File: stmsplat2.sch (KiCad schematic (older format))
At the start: 97 parts, among them J1 C11_2X36, J10 Conn_01x03_Male, J11 Conn_01x02_Male, J12 Conn_01x04_Male, J13 Conn_01x04_Male, J14 Conn_01x02, J15 Conn_01x02, J16 Screw_Terminal_01x03, J17 Screw_Terminal_01x02, J2 C12_2X36, J3 Conn_01x04_Male, J4 Conn_01x04_Male, J5 Conn_Coaxial, J6 Conn_01x06, J7 Conn_01x04_Male, J8 Conn_01x04_Male, J9 Conn_01x03_Male, Q1 BSS138LT1G, U1 ublox_chinese_PCB_module, U10 XCVR_E30-400M20S, U2 ESP32-C3-13, U3 SST25VF032B, U4 48L512-48LM01, U5 Opamp_Quad_MCP6024, U6 E180-ZG120A, U7 AZ1084C, U8 MCP6S93-X_UN, U9 DS2485

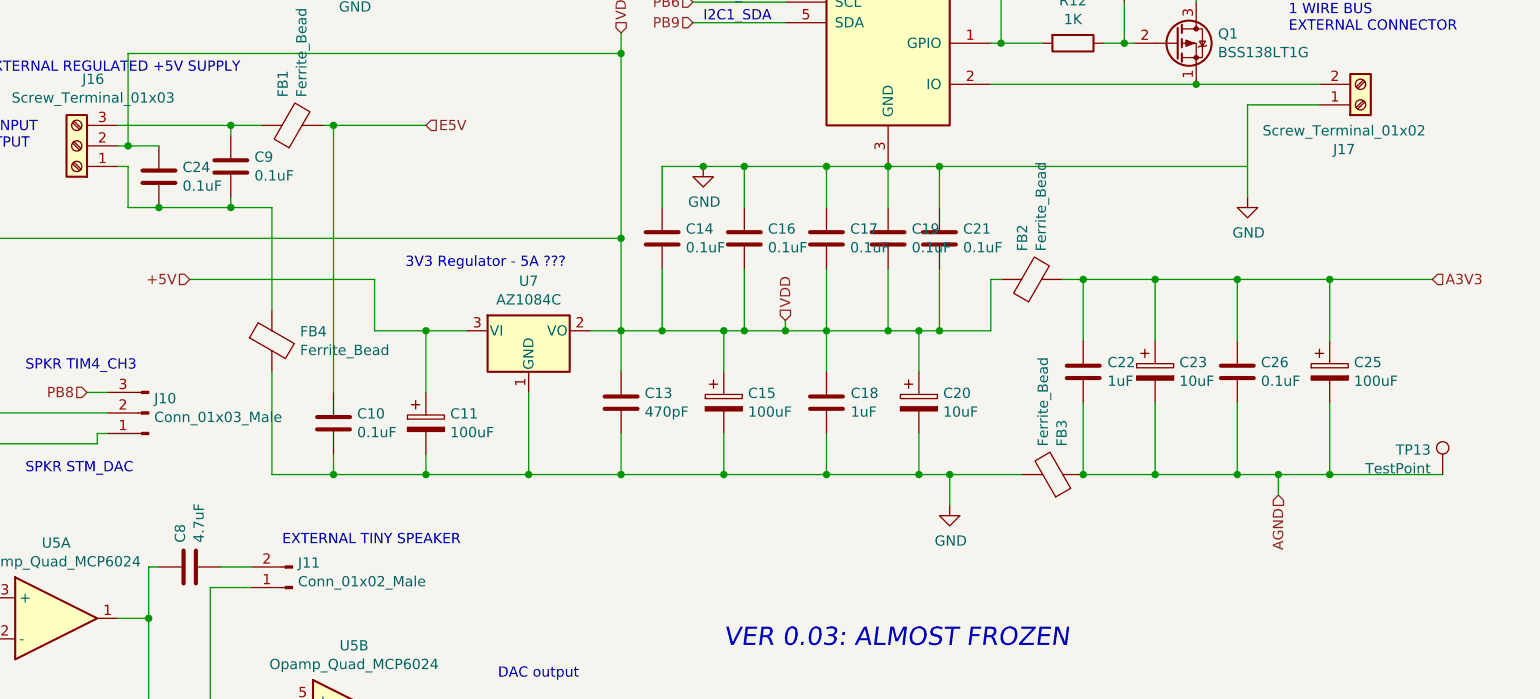
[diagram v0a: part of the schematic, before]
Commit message: changed all 0603 footprints to 0805 in the schematic
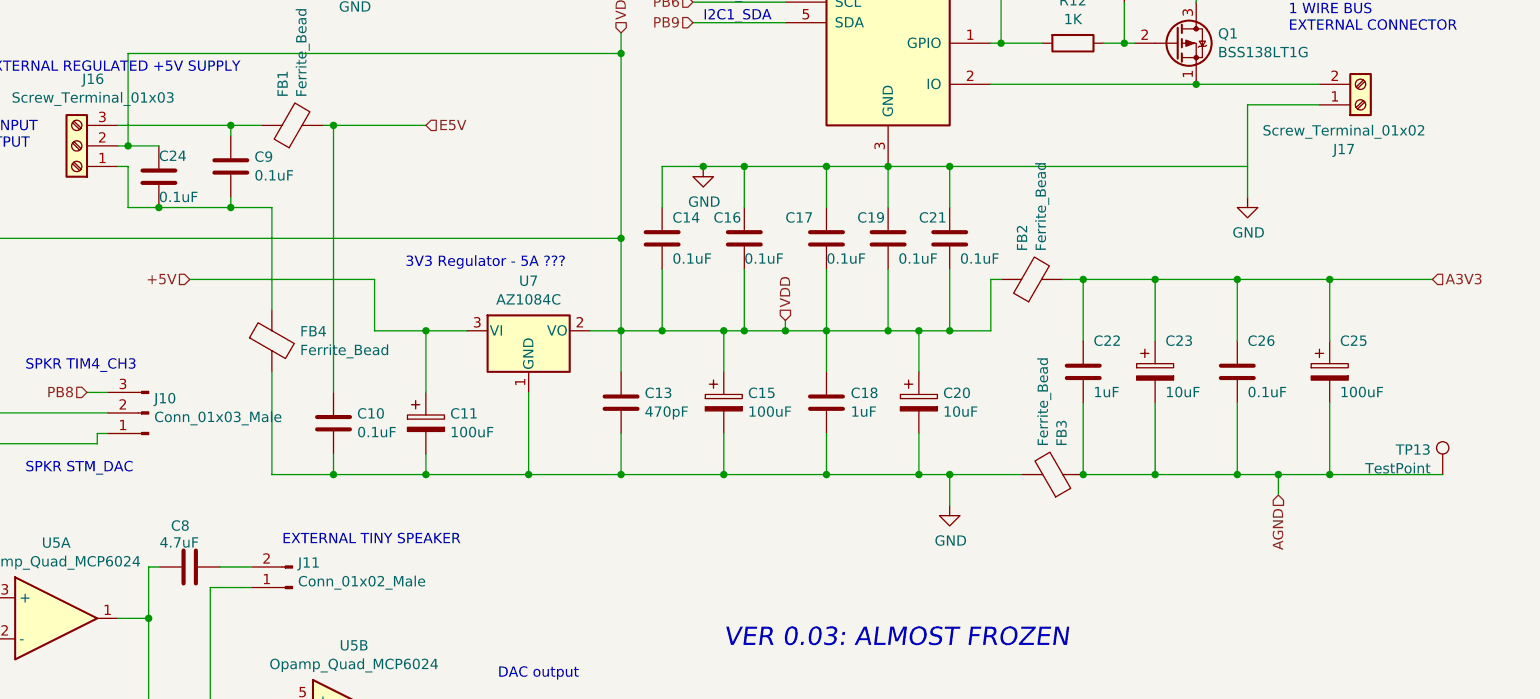
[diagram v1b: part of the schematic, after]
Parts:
- C1, C10, C14, C16, C17, C19, C21: footprint Capacitor_SMD:C_0603_1608Metric -> Capacitor_SMD:C_0805_2012Metric
- R1, R10, R11, R12, R13, R14, R2, R4, R7, R8, R9: footprint Resistor_SMD:R_0603_1608Metric -> Resistor_SMD:R_0805_2012Metric
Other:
- moved on the sheet: C21
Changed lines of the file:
@@
 U 1 1 5BE7E7BD
 P 14300 8950
-F 0 "C23" H 14418 8996 50  0000 L CNN
-F 1 "10uF" H 14418 8905 50  0000 L CNN
+F 0 "C23" H 14350 9100 50  0000 L CNN
+F 1 "10uF" H 14350 8850 50  0000 L CNN
 F 2 "Capacitor_THT:CP_Radial_D5.0mm_P2.50mm" H 14338 8800 50  0001 C CNN
 F 3 "~" H 14300 8950 50  0001 C CNN
@@
 U 1 1 5C39DBA4
 P 9600 9900
-F 0 "C8" H 9718 9946 50  0000 L CNN
-F 1 "4.7uF" H 9718 9855 50  0000 L CNN
+F 0 "C8" V 9800 9900 50  0000 L CNN
+F 1 "4.7uF" V 9718 9855 50  0000 L CNN
 F 2 "Capacitor_SMD:C_0805_2012Metric" H 9638 9750 50  0001 C CNN
 F 3 "~" H 9600 9900 50  0001 C CNN
@@
 F 0 "R13" H 14220 7046 50  0000 L CNN
 F 1 "100K" H 14220 6955 50  0000 L CNN
-F 2 "Resistor_SMD:R_0603_1608Metric" V 14080 7000 50  0001 C CNN
+F 2 "Resistor_SMD:R_0805_2012Metric" V 14080 7000 50  0001 C CNN
 F 3 "~" H 14150 7000 50  0001 C CNN
 	1    14150 7000
@@
 F 0 "R12" V 13693 7350 50  0000 C CNN
 F 1 "1K" V 13784 7350 50  0000 C CNN
-F 2 "Resistor_SMD:R_0603_1608Metric" V 13830 7350 50  0001 C CNN
+F 2 "Resistor_SMD:R_0805_2012Metric" V 13830 7350 50  0001 C CNN
 F 3 "~" H 13900 7350 50  0001 C CNN
 	1    13900 7350
@@
 SPI3 TRACKS TO BE KEPT SHORT AND EQUAL LENGTH
 Wire Wire Line
-	13250 8150 13250 7950
-Wire Wire Line
-	13250 8450 13250 8750
+	13300 8150 13300 7950
+Wire Wire Line
+	13300 8450 13300 8750
 Wire Wire Line
 	12200 8750 12300 8750
@@
 	13150 8950 13150 8750
 Connection ~ 13150 8750
-Connection ~ 13250 7950
-Wire Wire Line
-	13250 7950 14750 7950
-Wire Wire Line
-	13000 7950 13250 7950
-Wire Wire Line
-	13150 8750 13250 8750
-Wire Wire Line
-	13250 8750 13500 8750
-Connection ~ 13250 8750
+Wire Wire Line
+	13150 8750 13300 8750
+Wire Wire Line
+	13300 8750 13500 8750
+Connection ~ 13300 8750
 Wire Wire Line
 	13000 8150 13000 7950
@@
 F 0 "R1" H 1070 9946 50  0000 L CNN
 F 1 "4K7" H 1070 9855 50  0000 L CNN
-F 2 "Resistor_SMD:R_0603_1608Metric" V 930 9900 50  0001 C CNN
+F 2 "Resistor_SMD:R_0805_2012Metric" V 930 9900 50  0001 C CNN
 F 3 "~" H 1000 9900 50  0001 C CNN
 	1    1000 9900
@@
 F 0 "R2" H 6270 5146 50  0000 L CNN
 F 1 "3K3" H 6270 5055 50  0000 L CNN
-F 2 "Resistor_SMD:R_0603_1608Metric" V 6130 5100 50  0001 C CNN
+F 2 "Resistor_SMD:R_0805_2012Metric" V 6130 5100 50  0001 C CNN
 F 3 "~" H 6200 5100 50  0001 C CNN
 	1    6200 5100
@@
 F 0 "C1" H 1565 10096 50  0000 L CNN
 F 1 "0.1uF" H 1565 10005 50  0000 L CNN
-F 2 "Capacitor_SMD:C_0603_1608Metric" H 1488 9900 50  0001 C CNN
+F 2 "Capacitor_SMD:C_0805_2012Metric" H 1488 9900 50  0001 C CNN
 F 3 "~" H 1450 10050 50  0001 C CNN
 	1    1450 10050
@@
 F 0 "R11" H 12870 4296 50  0000 L CNN
 F 1 "470R" H 12870 4205 50  0000 L CNN
-F 2 "Resistor_SMD:R_0603_1608Metric" V 12730 4250 50  0001 C CNN
+F 2 "Resistor_SMD:R_0805_2012Metric" V 12730 4250 50  0001 C CNN
 F 3 "~" H 12800 4250 50  0001 C CNN
 	1    12800 4250
@@
 F 0 "R4" H 8020 6746 50  0000 L CNN
 F 1 "470R" H 8020 6655 50  0000 L CNN
-F 2 "Resistor_SMD:R_0603_1608Metric" V 7880 6700 50  0001 C CNN
+F 2 "Resistor_SMD:R_0805_2012Metric" V 7880 6700 50  0001 C CNN
 F 3 "~" H 7950 6700 50  0001 C CNN
 	1    7950 6700
@@
 F 0 "R14" H 15870 5846 50  0000 L CNN
 F 1 "470R" H 15870 5755 50  0000 L CNN
-F 2 "Resistor_SMD:R_0603_1608Metric" V 15730 5800 50  0001 C CNN
+F 2 "Resistor_SMD:R_0805_2012Metric" V 15730 5800 50  0001 C CNN
 F 3 "~" H 15800 5800 50  0001 C CNN
 	1    15800 5800
@@
 F 0 "R9" H 11920 2846 50  0000 L CNN
 F 1 "22K" H 11920 2755 50  0000 L CNN
-F 2 "Resistor_SMD:R_0603_1608Metric" V 11780 2800 50  0001 C CNN
+F 2 "Resistor_SMD:R_0805_2012Metric" V 11780 2800 50  0001 C CNN
 F 3 "~" H 11850 2800 50  0001 C CNN
 	1    11850 2800
@@
 F 0 "R10" H 11920 3246 50  0000 L CNN
 F 1 "10K" H 11920 3155 50  0000 L CNN
-F 2 "Resistor_SMD:R_0603_1608Metric" V 11780 3200 50  0001 C CNN
+F 2 "Resistor_SMD:R_0805_2012Metric" V 11780 3200 50  0001 C CNN
 F 3 "~" H 11850 3200 50  0001 C CNN
 	1    11850 3200
@@
 F 0 "R7" H 10620 996 50  0000 L CNN
 F 1 "4K7" H 10620 905 50  0000 L CNN
-F 2 "Resistor_SMD:R_0603_1608Metric" V 10480 950 50  0001 C CNN
+F 2 "Resistor_SMD:R_0805_2012Metric" V 10480 950 50  0001 C CNN
 F 3 "~" H 10550 950 50  0001 C CNN
 	1    10550 950
@@
 F 0 "R8" H 10620 1496 50  0000 L CNN
 F 1 "4K7" H 10620 1405 50  0000 L CNN
-F 2 "Resistor_SMD:R_0603_1608Metric" V 10480 1450 50  0001 C CNN
+F 2 "Resistor_SMD:R_0805_2012Metric" V 10480 1450 50  0001 C CNN
 F 3 "~" H 10550 1450 50  0001 C CNN
 	1    10550 1450
@@
 U 1 1 63187970
 P 11900 8300
-F 0 "C14" H 12015 8346 50  0000 L CNN
-F 1 "0.1uF" H 12015 8255 50  0000 L CNN
-F 2 "Capacitor_SMD:C_0603_1608Metric" H 11938 8150 50  0001 C CNN
+F 0 "C14" H 11950 8400 50  0000 L CNN
+F 1 "0.1uF" H 11950 8200 50  0000 L CNN
+F 2 "Capacitor_SMD:C_0805_2012Metric" H 11938 8150 50  0001 C CNN
 F 3 "~" H 11900 8300 50  0001 C CNN
 	1    11900 8300
@@
 U 1 1 63187C64
 P 12300 8300
-F 0 "C16" H 12415 8346 50  0000 L CNN
-F 1 "0.1uF" H 12415 8255 50  0000 L CNN
-F 2 "Capacitor_SMD:C_0603_1608Metric" H 12338 8150 50  0001 C CNN
+F 0 "C16" H 12150 8400 50  0000 L CNN
+F 1 "0.1uF" H 12300 8200 50  0000 L CNN
+F 2 "Capacitor_SMD:C_0805_2012Metric" H 12338 8150 50  0001 C CNN
 F 3 "~" H 12300 8300 50  0001 C CNN
 	1    12300 8300
@@
 U 1 1 63187D42
 P 12700 8300
-F 0 "C17" H 12815 8346 50  0000 L CNN
-F 1 "0.1uF" H 12815 8255 50  0000 L CNN
-F 2 "Capacitor_SMD:C_0603_1608Metric" H 12738 8150 50  0001 C CNN
+F 0 "C17" H 12500 8400 50  0000 L CNN
+F 1 "0.1uF" H 12700 8200 50  0000 L CNN
+F 2 "Capacitor_SMD:C_0805_2012Metric" H 12738 8150 50  0001 C CNN
 F 3 "~" H 12700 8300 50  0001 C CNN
 	1    12700 8300
@@
 U 1 1 63187E12
 P 13000 8300
-F 0 "C19" H 13115 8346 50  0000 L CNN
-F 1 "0.1uF" H 13115 8255 50  0000 L CNN
-F 2 "Capacitor_SMD:C_0603_1608Metric" H 13038 8150 50  0001 C CNN
+F 0 "C19" H 12850 8400 50  0000 L CNN
+F 1 "0.1uF" H 13050 8200 50  0000 L CNN
+F 2 "Capacitor_SMD:C_0805_2012Metric" H 13038 8150 50  0001 C CNN
 F 3 "~" H 13000 8300 50  0001 C CNN
 	1    13000 8300
@@
 L Device:C C21
 U 1 1 63187EDE
-P 13250 8300
-F 0 "C21" H 13365 8346 50  0000 L CNN
-F 1 "0.1uF" H 13365 8255 50  0000 L CNN
-F 2 "Capacitor_SMD:C_0603_1608Metric" H 13288 8150 50  0001 C CNN
-F 3 "~" H 13250 8300 50  0001 C CNN
-	1    13250 8300
+P 13300 8300
+F 0 "C21" H 13150 8400 50  0000 L CNN
+F 1 "0.1uF" H 13350 8200 50  0000 L CNN
+F 2 "Capacitor_SMD:C_0805_2012Metric" H 13338 8150 50  0001 C CNN
+F 3 "~" H 13300 8300 50  0001 C CNN
+	1    13300 8300
 	1    0    0    -1
 $EndComp
@@
 U 1 1 631889B9
 P 15150 8950
-F 0 "C25" H 15268 8996 50  0000 L CNN
-F 1 "100uF" H 15268 8905 50  0000 L CNN
+F 0 "C25" H 15200 9100 50  0000 L CNN
+F 1 "100uF" H 15200 8850 50  0000 L CNN
 F 2 "Capacitor_SMD:CP_Elec_8x10" H 15188 8800 50  0001 C CNN
 F 3 "~" H 15150 8950 50  0001 C CNN
@@
 U 1 1 635D69B8
 P 13950 8950
-F 0 "C22" H 14068 8996 50  0000 L CNN
-F 1 "1uF" H 14068 8905 50  0000 L CNN
+F 0 "C22" H 14000 9100 50  0000 L CNN
+F 1 "1uF" H 14000 8850 50  0000 L CNN
 F 2 "Capacitor_SMD:C_0402_1005Metric" H 13988 8800 50  0001 C CNN
 F 3 "~" H 13950 8950 50  0001 C CNN
@@
 F 0 "C10" H 10415 9246 50  0000 L CNN
 F 1 "0.1uF" H 10415 9155 50  0000 L CNN
-F 2 "Capacitor_SMD:C_0603_1608Metric" H 10338 9050 50  0001 C CNN
+F 2 "Capacitor_SMD:C_0805_2012Metric" H 10338 9050 50  0001 C CNN
 F 3 "~" H 10300 9200 50  0001 C CNN
 	1    10300 9200
@@
 U 1 1 61B65493
 P 14700 8950
-F 0 "C26" H 14815 8996 50  0000 L CNN
-F 1 "0.1uF" H 14815 8905 50  0000 L CNN
+F 0 "C26" H 14750 9100 50  0000 L CNN
+F 1 "0.1uF" H 14750 8850 50  0000 L CNN
 F 2 "Capacitor_SMD:C_0603_1608Metric" H 14738 8800 50  0001 C CNN
 F 3 "~" H 14700 8950 50  0001 C CNN
@@
 U 1 1 62741EFC
 P 9450 8000
-F 0 "C24" H 9565 8046 50  0000 L CNN
-F 1 "0.1uF" H 9565 7955 50  0000 L CNN
+F 0 "C24" H 9450 8100 50  0000 L CNN
+F 1 "0.1uF" H 9450 7900 50  0000 L CNN
 F 2 "Capacitor_SMD:C_0805_2012Metric_Pad1.15x1.40mm_HandSolder" H 9488 7850 50  0001 C CNN
 F 3 "~" H 9450 8000 50  0001 C CNN
@@
 Text Notes 1850 7950 0    50   ~ 0
 DEBUG/CONSOLE\nCOM PORT\n
+Connection ~ 13300 7950
+Wire Wire Line
+	13300 7950 14750 7950
+Wire Wire Line
+	13000 7950 13300 7950
 $EndSCHEMATC

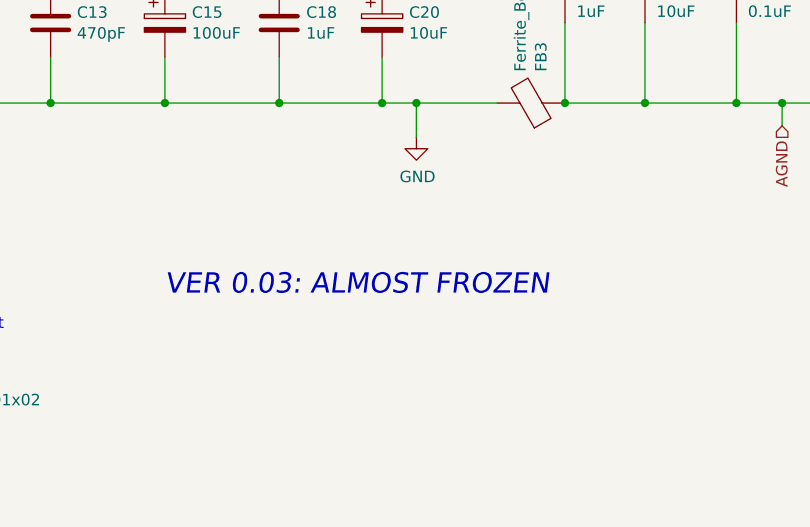
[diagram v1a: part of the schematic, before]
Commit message: forgot to bump Sch ver to 0.04
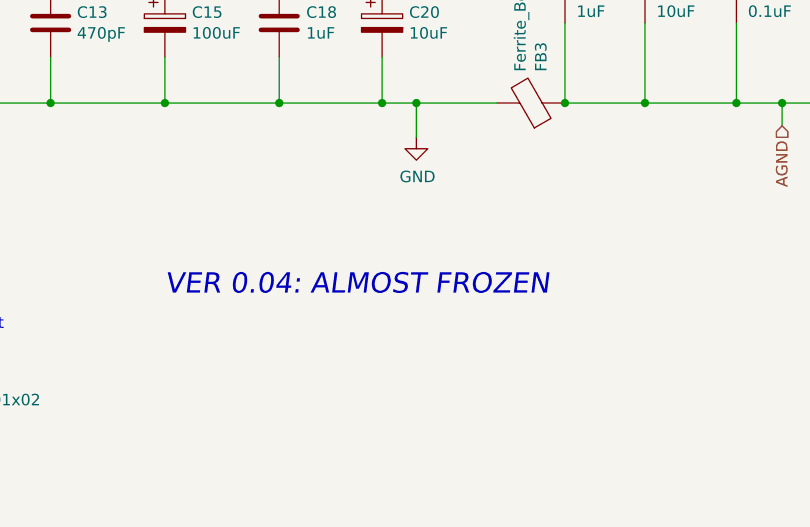
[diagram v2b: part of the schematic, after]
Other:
- note added: "VER 0.04: ALMOST FROZEN"
- note removed: "VER 0.03: ALMOST FROZEN"
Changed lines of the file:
@@
 SERIAL FLASH ROM\n  AND NVRAM
 Text Notes 12200 10300 0    89   Italic 0
-VER 0.03: ALMOST FROZEN
+VER 0.04: ALMOST FROZEN
 $Comp
 L Connector_Generic:Conn_01x02 J14

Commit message: ERC check resolution, resolved empty / unused nets
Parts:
- U2: value ESP32-C3-13 -> ESP-C3-13U
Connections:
- net E5V is gone; now on net +5V: C10.1, FB1.2, J1.6 (Pin_6)
- net AGND renamed GNDA
- net XB_PIO4: no longer names the net of RN1.7 (R2.2)
- no-connect marks 0 -> 78
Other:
- note added: "VER 0.05: ALMOST FROZEN - ERC Checks"
- note removed: "VER 0.04: ALMOST FROZEN"
- moved on the sheet: J1, J13, J15, J2, J7, J9
